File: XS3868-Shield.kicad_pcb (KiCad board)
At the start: 2 copper layers, 6 parts, among them P1 CONN_01X03, P2 CONN_01X02, U1 XS3868, U2 AP111733

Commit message: PCB done
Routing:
- net GND: track 0.00 -> 20.0 mm
- net Net-(P1-Pad3): track 0.00 -> 18.2 mm
- net Net-(P1-Pad2): track 0.00 -> 16.7 mm
- net +3V3: track 0.00 -> 15.6 mm
- net Net-(P1-Pad1): track 0.00 -> 15.1 mm
- net +12V: track 0.00 -> 7.44 mm
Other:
- board outline added: 33 x 34.3 mm
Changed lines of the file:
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@@
-(kicad_pcb (version 20160815) (host pcbnew no-vcs-found-7434~57~ubuntu16.04.1)
+(kicad_pcb (version 4) (host pcbnew 4.0.4-stable)
   (general
     (links 12)
     (no_connects 12)
-    (area 0 0 0 0)
+    (area 83.744999 31.674999 116.915001 66.115001)
     (thickness 1.6)
-    (drawings 0)
-    (tracks 0)
+    (drawings 6)
+    (tracks 34)
     (zones 0)
     (modules 6)
@@
     (pad_to_mask_clearance 0.2)
     (aux_axis_origin 0 0)
-    (visible_elements FFFFFF7F)
+    (visible_elements 7FFFFFFF)
     (pcbplotparams
       (layerselection 0x00030_ffffffff)
@@
       (hpglpenspeed 20)
       (hpglpendiameter 15)
+      (hpglpenoverlay 2)
       (psnegative false)
       (psa4output false)
@@
     )
   )
+  (dimension 34.29 (width 0.3) (layer Dwgs.User)
+    (gr_text "34,290 mm" (at 123.27 48.895 270) (layer Dwgs.User)
+      (effects (font (size 1.5 1.5) (thickness 0.3)))
+    )
+    (feature1 (pts (xy 116.84 66.04) (xy 124.62 66.04)))
+    (feature2 (pts (xy 116.84 31.75) (xy 124.62 31.75)))
+    (crossbar (pts (xy 121.92 31.75) (xy 121.92 66.04)))
+    (arrow1a (pts (xy 121.92 66.04) (xy 121.333579 64.913496)))
+    (arrow1b (pts (xy 121.92 66.04) (xy 122.506421 64.913496)))
+    (arrow2a (pts (xy 121.92 31.75) (xy 121.333579 32.876504)))
+    (arrow2b (pts (xy 121.92 31.75) (xy 122.506421 32.876504)))
+  )
+  (dimension 33.02 (width 0.3) (layer Dwgs.User)
+    (gr_text "33,020 mm" (at 100.33 26.59) (layer Dwgs.User)
+      (effects (font (size 1.5 1.5) (thickness 0.3)))
+    )
+    (feature1 (pts (xy 116.84 31.75) (xy 116.84 25.24)))
+    (feature2 (pts (xy 83.82 31.75) (xy 83.82 25.24)))
+    (crossbar (pts (xy 83.82 27.94) (xy 116.84 27.94)))
+    (arrow1a (pts (xy 116.84 27.94) (xy 115.713496 28.526421)))
+    (arrow1b (pts (xy 116.84 27.94) (xy 115.713496 27.353579)))
+    (arrow2a (pts (xy 83.82 27.94) (xy 84.946504 28.526421)))
+    (arrow2b (pts (xy 83.82 27.94) (xy 84.946504 27.353579)))
+  )
+  (gr_line (start 83.82 31.75) (end 83.82 66.04) (layer Edge.Cuts) (width 0.15))
+  (gr_line (start 116.84 31.75) (end 83.82 31.75) (layer Edge.Cuts) (width 0.15))
+  (gr_line (start 116.84 66.04) (end 116.84 31.75) (layer Edge.Cuts) (width 0.15))
+  (gr_line (start 83.82 66.04) (end 116.84 66.04) (layer Edge.Cuts) (width 0.15))
+  (segment (start 86.6 55.27) (end 86.6 52.91) (width 0.6) (layer F.Cu) (net 1))
+  (segment (start 86.6 52.91) (end 87.059 52.451) (width 0.6) (layer F.Cu) (net 1))
+  (segment (start 87.059 52.451) (end 87.059 48.831) (width 0.6) (layer F.Cu) (net 1))
+  (segment (start 87.059 48.831) (end 87.63 48.26) (width 0.6) (layer F.Cu) (net 1))
+  (segment (start 94.234 57.563) (end 93.493 57.563) (width 0.6) (layer F.Cu) (net 2))
+  (segment (start 93.493 57.563) (end 91.2 55.27) (width 0.6) (layer F.Cu) (net 2))
+  (segment (start 91.059 52.451) (end 91.059 55.129) (width 0.6) (layer F.Cu) (net 2))
+  (segment (start 91.059 55.129) (end 91.2 55.27) (width 0.6) (layer F.Cu) (net 2))
+  (segment (start 97.79 59.35) (end 96.021 59.35) (width 0.6) (layer F.Cu) (net 2))
+  (segment (start 96.021 59.35) (end 94.234 57.563) (width 0.6) (layer F.Cu) (net 2))
+  (segment (start 87.63 45.72) (end 88.832081 45.72) (width 0.6) (layer F.Cu) (net 2))
+  (segment (start 88.832081 45.72) (end 91.059 47.946919) (width 0.6) (layer F.Cu) (net 2))
+  (segment (start 91.059 47.946919) (end 91.059 52.451) (width 0.6) (layer F.Cu) (net 2))
+  (segment (start 97.79 60.65) (end 95.147 60.65) (width 0.6) (layer F.Cu) (net 3))
+  (segment (start 95.147 60.65) (end 94.234 61.563) (width 0.6) (layer F.Cu) (net 3))
+  (segment (start 88.9 61.57) (end 94.227 61.57) (width 0.6) (layer F.Cu) (net 3))
+  (segment (start 94.227 61.57) (end 94.234 61.563) (width 0.6) (layer F.Cu) (net 3))
+  (segment (start 88.9 55.27) (end 88.9 56.87) (width 0.6) (layer F.Cu) (net 3))
+  (segment (start 88.9 56.87) (end 88.9 61.57) (width 0.6) (layer F.Cu) (net 3))
+  (segment (start 97.79 47.65) (end 95.974164 47.65) (width 0.6) (layer F.Cu) (net 4))
+  (segment (start 95.974164 47.65) (end 94.3 45.975836) (width 0.6) (layer F.Cu) (net 4))
+  (segment (start 94.3 45.975836) (end 94.3 39.89) (width 0.6) (layer F.Cu) (net 4))
+  (segment (start 94.3 39.89) (end 91.24 36.83) (width 0.6) (layer F.Cu) (net 4))
+  (segment (start 91.24 36.83) (end 87.63 36.83) (width 0.6) (layer F.Cu) (net 4))
+  (segment (start 97.79 48.95) (end 95.899626 48.95) (width 0.6) (layer F.Cu) (net 5))
+  (segment (start 95.899626 48.95) (end 92.92 45.970374) (width 0.6) (layer F.Cu) (net 5))
+  (segment (start 92.92 45.970374) (end 92.92 41.65) (width 0.6) (layer F.Cu) (net 5))
+  (segment (start 92.92 41.65) (end 90.64 39.37) (width 0.6) (layer F.Cu) (net 5))
+  (segment (start 90.64 39.37) (end 87.63 39.37) (width 0.6) (layer F.Cu) (net 5))
+  (segment (start 97.79 50.25) (end 95.733453 50.25) (width 0.6) (layer F.Cu) (net 6))
+  (segment (start 95.733453 50.25) (end 91.7 46.216547) (width 0.6) (layer F.Cu) (net 6))
+  (segment (start 91.7 46.216547) (end 91.7 43.68) (width 0.6) (layer F.Cu) (net 6))
+  (segment (start 91.7 43.68) (end 89.93 41.91) (width 0.6) (layer F.Cu) (net 6))
+  (segment (start 89.93 41.91) (end 87.63 41.91) (width 0.6) (layer F.Cu) (net 6))
 )

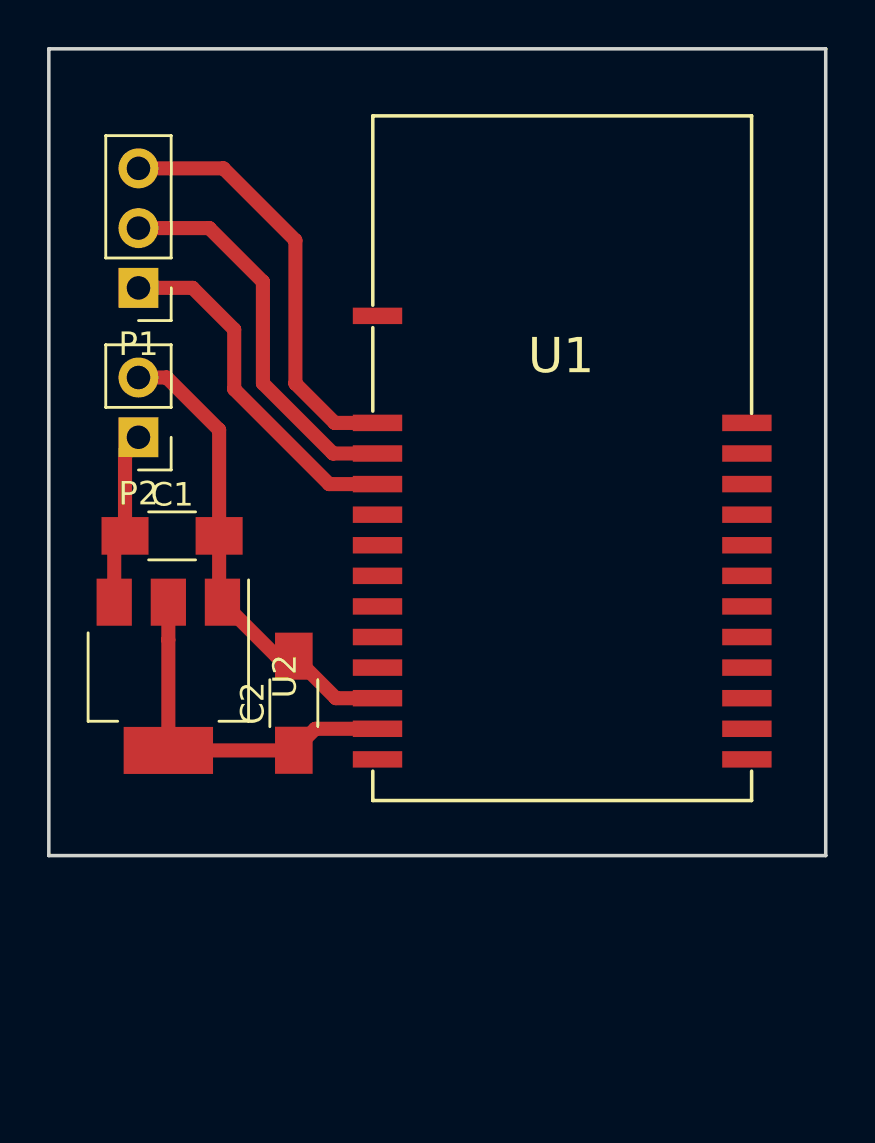
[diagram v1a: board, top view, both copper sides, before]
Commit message: Added ground plane
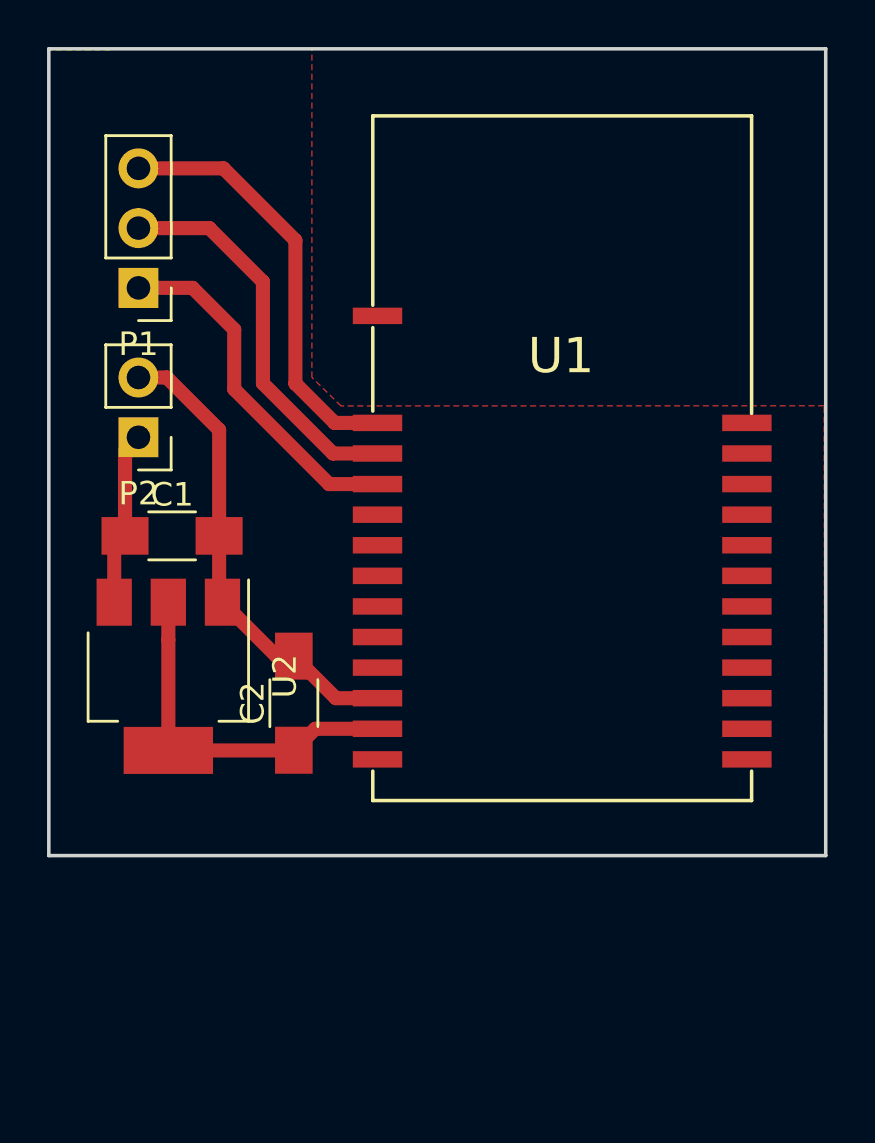
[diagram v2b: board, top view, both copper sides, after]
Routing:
- added copper zone on F.Cu, net GND
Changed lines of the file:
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@@
   (general
     (links 12)
-    (no_connects 12)
+    (no_connects 0)
     (area 83.744999 31.674999 116.915001 66.115001)
     (thickness 1.6)
@@
     (trace_clearance 0.2)
     (zone_clearance 0.508)
-    (zone_45_only no)
+    (zone_45_only yes)
     (trace_min 0.2)
     (segment_width 0.2)
@@
   (gr_line (start 116.84 66.04) (end 116.84 31.75) (layer Edge.Cuts) (width 0.15))
   (gr_line (start 83.82 66.04) (end 116.84 66.04) (layer Edge.Cuts) (width 0.15))
+  (segment (start 87.059 48.831) (end 87.63 48.26) (width 0.6) (layer F.Cu) (net 1))
   (segment (start 86.6 55.27) (end 86.6 52.91) (width 0.6) (layer F.Cu) (net 1))
   (segment (start 86.6 52.91) (end 87.059 52.451) (width 0.6) (layer F.Cu) (net 1))
   (segment (start 87.059 52.451) (end 87.059 48.831) (width 0.6) (layer F.Cu) (net 1))
-  (segment (start 87.059 48.831) (end 87.63 48.26) (width 0.6) (layer F.Cu) (net 1))
+  (segment (start 87.63 45.72) (end 88.832081 45.72) (width 0.6) (layer F.Cu) (net 2))
+  (segment (start 88.832081 45.72) (end 91.059 47.946919) (width 0.6) (layer F.Cu) (net 2))
+  (segment (start 91.059 47.946919) (end 91.059 52.451) (width 0.6) (layer F.Cu) (net 2))
   (segment (start 94.234 57.563) (end 93.493 57.563) (width 0.6) (layer F.Cu) (net 2))
   (segment (start 93.493 57.563) (end 91.2 55.27) (width 0.6) (layer F.Cu) (net 2))
@@
   (segment (start 97.79 59.35) (end 96.021 59.35) (width 0.6) (layer F.Cu) (net 2))
   (segment (start 96.021 59.35) (end 94.234 57.563) (width 0.6) (layer F.Cu) (net 2))
-  (segment (start 87.63 45.72) (end 88.832081 45.72) (width 0.6) (layer F.Cu) (net 2))
-  (segment (start 88.832081 45.72) (end 91.059 47.946919) (width 0.6) (layer F.Cu) (net 2))
-  (segment (start 91.059 47.946919) (end 91.059 52.451) (width 0.6) (layer F.Cu) (net 2))
   (segment (start 97.79 60.65) (end 95.147 60.65) (width 0.6) (layer F.Cu) (net 3))
   (segment (start 95.147 60.65) (end 94.234 61.563) (width 0.6) (layer F.Cu) (net 3))
@@
   (segment (start 88.9 55.27) (end 88.9 56.87) (width 0.6) (layer F.Cu) (net 3))
   (segment (start 88.9 56.87) (end 88.9 61.57) (width 0.6) (layer F.Cu) (net 3))
+  (segment (start 94.3 39.89) (end 91.24 36.83) (width 0.6) (layer F.Cu) (net 4))
+  (segment (start 91.24 36.83) (end 87.63 36.83) (width 0.6) (layer F.Cu) (net 4))
   (segment (start 97.79 47.65) (end 95.974164 47.65) (width 0.6) (layer F.Cu) (net 4))
   (segment (start 95.974164 47.65) (end 94.3 45.975836) (width 0.6) (layer F.Cu) (net 4))
   (segment (start 94.3 45.975836) (end 94.3 39.89) (width 0.6) (layer F.Cu) (net 4))
-  (segment (start 94.3 39.89) (end 91.24 36.83) (width 0.6) (layer F.Cu) (net 4))
-  (segment (start 91.24 36.83) (end 87.63 36.83) (width 0.6) (layer F.Cu) (net 4))
+  (segment (start 90.64 39.37) (end 87.63 39.37) (width 0.6) (layer F.Cu) (net 5))
+  (segment (start 92.92 41.65) (end 90.64 39.37) (width 0.6) (layer F.Cu) (net 5))
   (segment (start 97.79 48.95) (end 95.899626 48.95) (width 0.6) (layer F.Cu) (net 5))
   (segment (start 95.899626 48.95) (end 92.92 45.970374) (width 0.6) (layer F.Cu) (net 5))
   (segment (start 92.92 45.970374) (end 92.92 41.65) (width 0.6) (layer F.Cu) (net 5))
-  (segment (start 92.92 41.65) (end 90.64 39.37) (width 0.6) (layer F.Cu) (net 5))
-  (segment (start 90.64 39.37) (end 87.63 39.37) (width 0.6) (layer F.Cu) (net 5))
+  (segment (start 89.93 41.91) (end 87.63 41.91) (width 0.6) (layer F.Cu) (net 6))
+  (segment (start 91.7 43.68) (end 89.93 41.91) (width 0.6) (layer F.Cu) (net 6))
   (segment (start 97.79 50.25) (end 95.733453 50.25) (width 0.6) (layer F.Cu) (net 6))
   (segment (start 95.733453 50.25) (end 91.7 46.216547) (width 0.6) (layer F.Cu) (net 6))
   (segment (start 91.7 46.216547) (end 91.7 43.68) (width 0.6) (layer F.Cu) (net 6))
-  (segment (start 91.7 43.68) (end 89.93 41.91) (width 0.6) (layer F.Cu) (net 6))
-  (segment (start 89.93 41.91) (end 87.63 41.91) (width 0.6) (layer F.Cu) (net 6))
+  (zone (net 0) (net_name "") (layer F.Cu) (hatch edge 0.508)
+    (connect_pads (clearance 0.508))
+    (min_thickness 0.254)
+    (keepout (tracks not_allowed) (vias not_allowed) (copperpour allowed))
+    (fill (arc_segments 16) (thermal_gap 0.508) (thermal_bridge_width 0.508))
+    (polygon
+      (pts
+        (xy 95 31.75) (xy 95 45) (xy 95.01124 45.70984) (xy 96.22028 46.92396) (xy 116.72316 46.92396)
+        (xy 116.75872 31.7754) (xy 95.00108 31.75)
+      )
+    )
+  )
+  (zone (net 2) (net_name GND) (layer F.Cu) (hatch edge 0.508)
+    (connect_pads (clearance 0.508))
+    (min_thickness 0.254)
+    (fill yes (arc_segments 32) (thermal_gap 0.508) (thermal_bridge_width 0.508))
+    (polygon
+      (pts
+        (xy 83.8 31.8) (xy 83.8 66) (xy 116.8 66) (xy 116.77142 46.92142) (xy 96.23806 46.92904)
+        (xy 95.00108 45.71492) (xy 95.00108 31.75254)
+      )
+    )
+  )
 )

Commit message: Layout review
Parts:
- added C3: 100u, SMD_Packages:SMD-2512_Pol, F.Cu at (112.7, 68.9)
- added U3: LM7805, RACE_UP_ED:LM7805_TO92, B.Cu at (93.2, 72.2)
- C1, C2: footprint Capacitors_SMD:C_1206_HandSoldering -> SMD_Packages:SMD-2512_Pol
- moved U2 19.8 mm to (105.7, 68.9)
- moved P2 13.1 mm to (88.9, 61.3)
- moved C2 10.3 mm to (98.5, 68.9)
- moved P1 9.66 mm to (88.9, 51.5)
- moved C1 9.10 mm to (93.3, 60.5), turned to 90 degrees
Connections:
- C2 pad 1: +3V3 -> +5V
- U1 pad 1: Net-(U1-Pad1) -> (no net)
- U1 pad 10: Net-(U1-Pad10) -> (no net)
- U1 pad 13: Net-(U1-Pad13) -> (no net)
- U1 pad 14: Net-(U1-Pad14) -> (no net)
- U1 pad 15: Net-(U1-Pad15) -> (no net)
- U1 pad 16: Net-(U1-Pad16) -> (no net)
- U1 pad 17: Net-(U1-Pad17) -> (no net)
- U1 pad 18: Net-(U1-Pad18) -> (no net)
- U1 pad 19: Net-(U1-Pad19) -> (no net)
- U1 pad 20: Net-(U1-Pad20) -> (no net)
- U1 pad 21: Net-(U1-Pad21) -> (no net)
- U1 pad 22: Net-(U1-Pad22) -> (no net)
- U1 pad 23: Net-(U1-Pad23) -> (no net)
- U1 pad 24: Net-(U1-Pad24) -> (no net)
- U1 pad 25: Net-(U1-Pad25) -> (no net)
- U1 pad 5: Net-(U1-Pad5) -> (no net)
- U1 pad 6: Net-(U1-Pad6) -> (no net)
- U1 pad 7: Net-(U1-Pad7) -> (no net)
- U1 pad 8: Net-(U1-Pad8) -> (no net)
- U1 pad 9: Net-(U1-Pad9) -> (no net)
- U2 pad 3: +12V -> +5V
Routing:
- net +5V: track 0.00 -> 12.5 mm
- net Net-(P1-Pad3): track 18.2 -> 9.41 mm
- net +3V3: track 15.6 -> 24.3 mm
- net Net-(P1-Pad2): track 16.7 -> 8.89 mm
- net Net-(P1-Pad1): track 15.1 -> 9.41 mm
- net +12V: track 7.44 -> 11.3 mm
- net GND: track 20.0 -> 17.5 mm
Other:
- board size 33 x 34.3 mm -> 30.5 x 43.2 mm
